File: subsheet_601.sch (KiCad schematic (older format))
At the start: 11 parts, among them P600 10K ×8, U632 74LS244_PHY

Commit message: Resolves #1 : Use 4-resistor packs wherever it is possible
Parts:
- removed P600: 10K ×8, Resistor_THT:R_Array_SIP9, symbol Device:R_Network08_US
- added RN? (x2): 10K ×8, symbol custom_passives:R_Pack04_US
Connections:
- wire segments 47 -> 62
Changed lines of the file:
@@
 	1    0    0    -1
 $EndComp
-$Comp
-L Device:R_Network08_US P600
-U 1 1 60D5E0A1
-P 5400 4400
-F 0 "P600" V 4900 4400 50  0000 C CNN
-F 1 "10K ×8" V 5800 4400 50  0000 C CNN
-F 2 "Resistor_THT:R_Array_SIP9" V 5875 4400 50  0001 C CNN
-F 3 "http://www.vishay.com/docs/31509/csc.pdf" H 5400 4400 50  0001 C CNN
-	1    5400 4400
-	0    1    1    0
-$EndComp
-Text Label 5800 4000 2    50   ~ 0
-VCC
-Text Label 5000 4000 0    50   ~ 0
+Text Label 4900 4000 0    50   ~ 0
 e0
-Text Label 5000 4100 0    50   ~ 0
+Text Label 4900 4100 0    50   ~ 0
 e1
-Text Label 5000 4200 0    50   ~ 0
+Text Label 4900 4200 0    50   ~ 0
 e2
-Text Label 5000 4300 0    50   ~ 0
+Text Label 4900 4300 0    50   ~ 0
 e3
-Text Label 5000 4400 0    50   ~ 0
+Text Label 4900 4700 0    50   ~ 0
 e4
-Text Label 5000 4500 0    50   ~ 0
+Text Label 4900 4800 0    50   ~ 0
 e5
-Text Label 5000 4600 0    50   ~ 0
+Text Label 4900 4900 0    50   ~ 0
 e6
-Text Label 5000 4700 0    50   ~ 0
+Text Label 4900 5000 0    50   ~ 0
 e7
 Wire Wire Line
-	5000 4000 5200 4000
-Wire Wire Line
-	5000 4100 5200 4100
-Wire Wire Line
-	5000 4200 5200 4200
-Wire Wire Line
-	5000 4300 5200 4300
-Wire Wire Line
-	5000 4400 5200 4400
-Wire Wire Line
-	5000 4500 5200 4500
-Wire Wire Line
-	5000 4600 5200 4600
-Wire Wire Line
-	5000 4700 5200 4700
-Wire Wire Line
-	5600 4000 5800 4000
+	4900 4000 5100 4000
+Wire Wire Line
+	4900 4100 5100 4100
+Wire Wire Line
+	4900 4200 5100 4200
+Wire Wire Line
+	4900 4300 5100 4300
+Wire Wire Line
+	4900 4700 5100 4700
+Wire Wire Line
+	4900 4800 5100 4800
+Wire Wire Line
+	4900 4900 5100 4900
+Wire Wire Line
+	4900 5000 5100 5000
 $Comp
 L Jumper:SolderJumper_2_Open E0
@@
 Wire Wire Line
 	7000 2650 7000 2850
+$Comp
+L custom_passives:R_Pack04_US RN?
+U 1 1 62582FB7
+P 5300 4200
+F 0 "RN?" V 5000 4200 50  0000 C CNN
+F 1 "10K ×8" V 5500 4200 50  0000 C CNN
+F 2 "" V 5575 4200 50  0001 C CNN
+F 3 "~" H 5300 4200 50  0001 C CNN
+	1    5300 4200
+	0    1    1    0
+$EndComp
+Text Label 5800 4000 2    50   ~ 0
+VCC
+Wire Wire Line
+	5500 4000 5600 4000
+Wire Wire Line
+	5500 4300 5600 4300
+Wire Wire Line
+	5600 4300 5600 4200
+Connection ~ 5600 4000
+Wire Wire Line
+	5600 4000 5800 4000
+Wire Wire Line
+	5500 4200 5600 4200
+Connection ~ 5600 4200
+Wire Wire Line
+	5600 4200 5600 4100
+Wire Wire Line
+	5500 4100 5600 4100
+Connection ~ 5600 4100
+Wire Wire Line
+	5600 4100 5600 4000
+$Comp
+L custom_passives:R_Pack04_US RN?
+U 1 1 625854E7
+P 5300 4900
+F 0 "RN?" V 5000 4900 50  0000 C CNN
+F 1 "10K ×8" V 5500 4900 50  0000 C CNN
+F 2 "" V 5575 4900 50  0001 C CNN
+F 3 "~" H 5300 4900 50  0001 C CNN
+	1    5300 4900
+	0    1    1    0
+$EndComp
+Text Label 5800 4700 2    50   ~ 0
+VCC
+Wire Wire Line
+	5500 4700 5600 4700
+Wire Wire Line
+	5500 5000 5600 5000
+Wire Wire Line
+	5600 5000 5600 4900
+Connection ~ 5600 4700
+Wire Wire Line
+	5600 4700 5800 4700
+Wire Wire Line
+	5500 4900 5600 4900
+Connection ~ 5600 4900
+Wire Wire Line
+	5600 4900 5600 4800
+Wire Wire Line
+	5500 4800 5600 4800
+Connection ~ 5600 4800
+Wire Wire Line
+	5600 4800 5600 4700
 $EndSCHEMATC

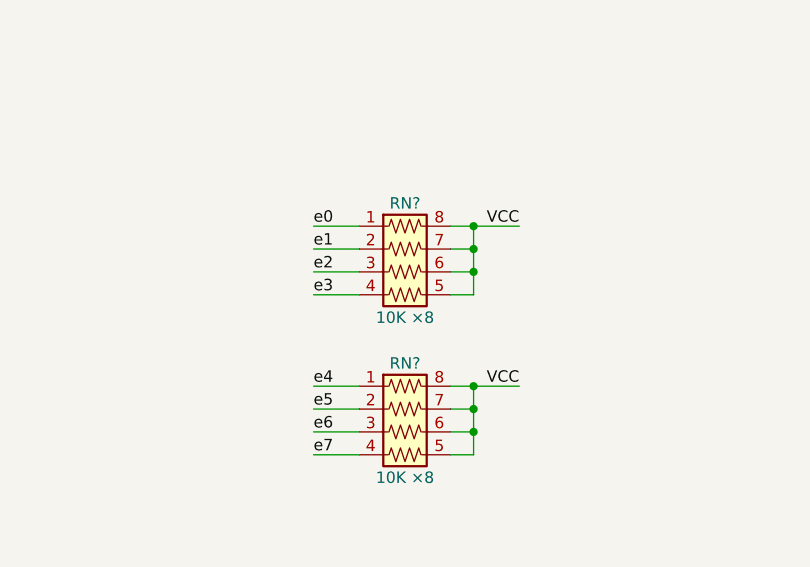
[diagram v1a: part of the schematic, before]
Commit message: annotate resistor networks and mark unused pins as unconnected
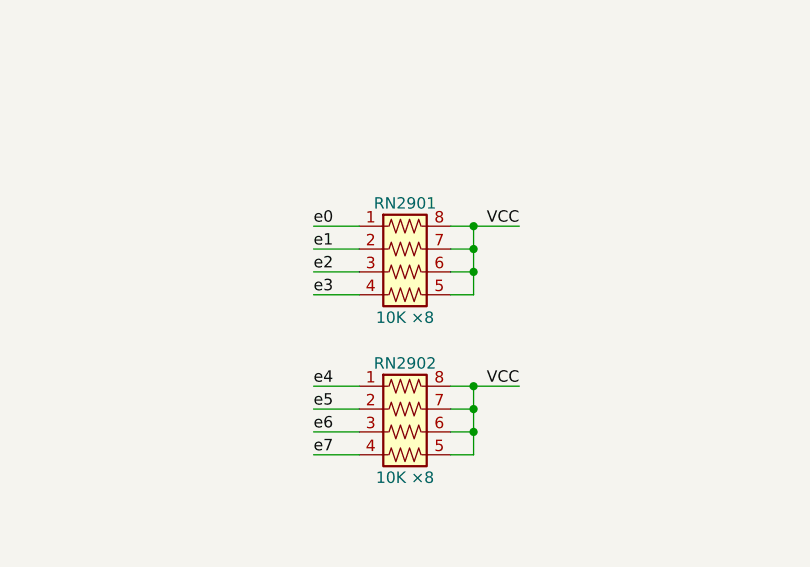
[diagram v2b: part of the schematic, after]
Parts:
- gave numbers to parts that had none: 2
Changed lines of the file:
@@
 	7000 2650 7000 2850
 $Comp
-L custom_passives:R_Pack04_US RN?
+L custom_passives:R_Pack04_US RN2901
 U 1 1 62582FB7
 P 5300 4200
-F 0 "RN?" V 5000 4200 50  0000 C CNN
+F 0 "RN2901" V 5000 4200 50  0000 C CNN
 F 1 "10K ×8" V 5500 4200 50  0000 C CNN
 F 2 "" V 5575 4200 50  0001 C CNN
@@
 	5600 4100 5600 4000
 $Comp
-L custom_passives:R_Pack04_US RN?
+L custom_passives:R_Pack04_US RN2902
 U 1 1 625854E7
 P 5300 4900
-F 0 "RN?" V 5000 4900 50  0000 C CNN
+F 0 "RN2902" V 5000 4900 50  0000 C CNN
 F 1 "10K ×8" V 5500 4900 50  0000 C CNN
 F 2 "" V 5575 4900 50  0001 C CNN

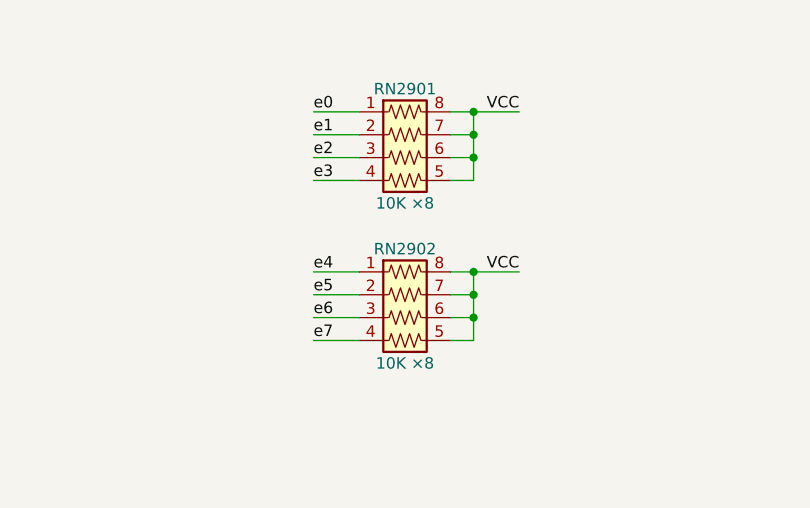
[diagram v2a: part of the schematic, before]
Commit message: Resolves #7 : Assign SMD footprints to resistors pack
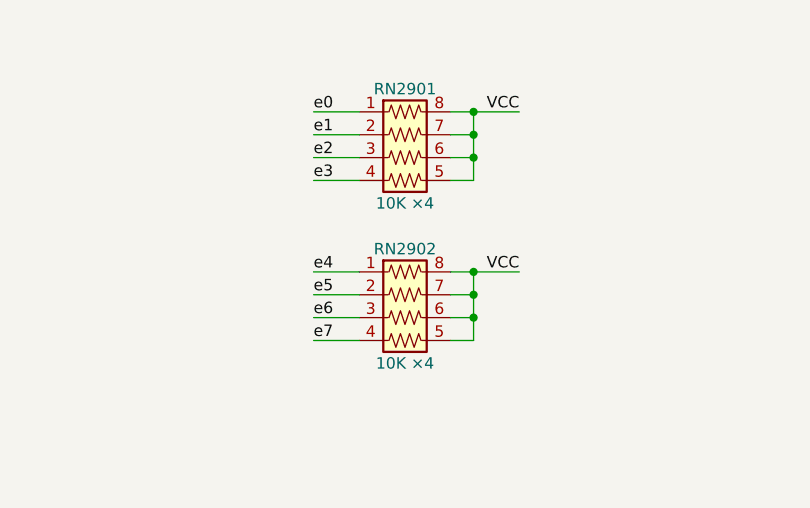
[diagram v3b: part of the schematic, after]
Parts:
- RN2901, RN2902: value 10K ×8 -> 10K ×4; footprint (none) -> Resistor_SMD:R_Array_Convex_4x0603
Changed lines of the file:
@@
 P 5300 4200
 F 0 "RN2901" V 5000 4200 50  0000 C CNN
-F 1 "10K ×8" V 5500 4200 50  0000 C CNN
-F 2 "" V 5575 4200 50  0001 C CNN
+F 1 "10K ×4" V 5500 4200 50  0000 C CNN
+F 2 "Resistor_SMD:R_Array_Convex_4x0603" V 5575 4200 50  0001 C CNN
 F 3 "~" H 5300 4200 50  0001 C CNN
 	1    5300 4200
@@
 P 5300 4900
 F 0 "RN2902" V 5000 4900 50  0000 C CNN
-F 1 "10K ×8" V 5500 4900 50  0000 C CNN
-F 2 "" V 5575 4900 50  0001 C CNN
+F 1 "10K ×4" V 5500 4900 50  0000 C CNN
+F 2 "Resistor_SMD:R_Array_Convex_4x0603" V 5575 4900 50  0001 C CNN
 F 3 "~" H 5300 4900 50  0001 C CNN
 	1    5300 4900

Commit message: Resolves #8 : Assign 1206 hand-solder footprints to non polarized capacitors
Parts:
- C632: footprint commons_passives_THT:Passive_THT_capacitor_mlcc_W2.54mm_L7.62mm -> Capacitor_SMD:C_1206_3216Metric_Pad1.33x1.80mm_HandSolder
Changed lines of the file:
@@
 F 0 "C632" H 7025 2600 50  0000 L CNN
 F 1 "0.1uF" H 7025 2400 50  0000 L CNN
-F 2 "commons_passives_THT:Passive_THT_capacitor_mlcc_W2.54mm_L7.62mm" H 7038 2350 50  0001 C CNN
+F 2 "Capacitor_SMD:C_1206_3216Metric_Pad1.33x1.80mm_HandSolder" H 7038 2350 50  0001 C CNN
 F 3 "~" H 7000 2500 50  0001 C CNN
 	1    7000 2500
